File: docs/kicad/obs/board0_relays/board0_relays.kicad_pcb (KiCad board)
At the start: 2 copper layers, 100.3 x 91.4 mm, 45 parts, among them J1 INST_POWER, J10 12V_TEST, J11 5V_TEST, J12 SN65HVD230, J13 CAN_TERMINATOR, J14 MAX3232, J15 GPS_IN, J2 NMEA2000, J3 NMEA2000, J4 83A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

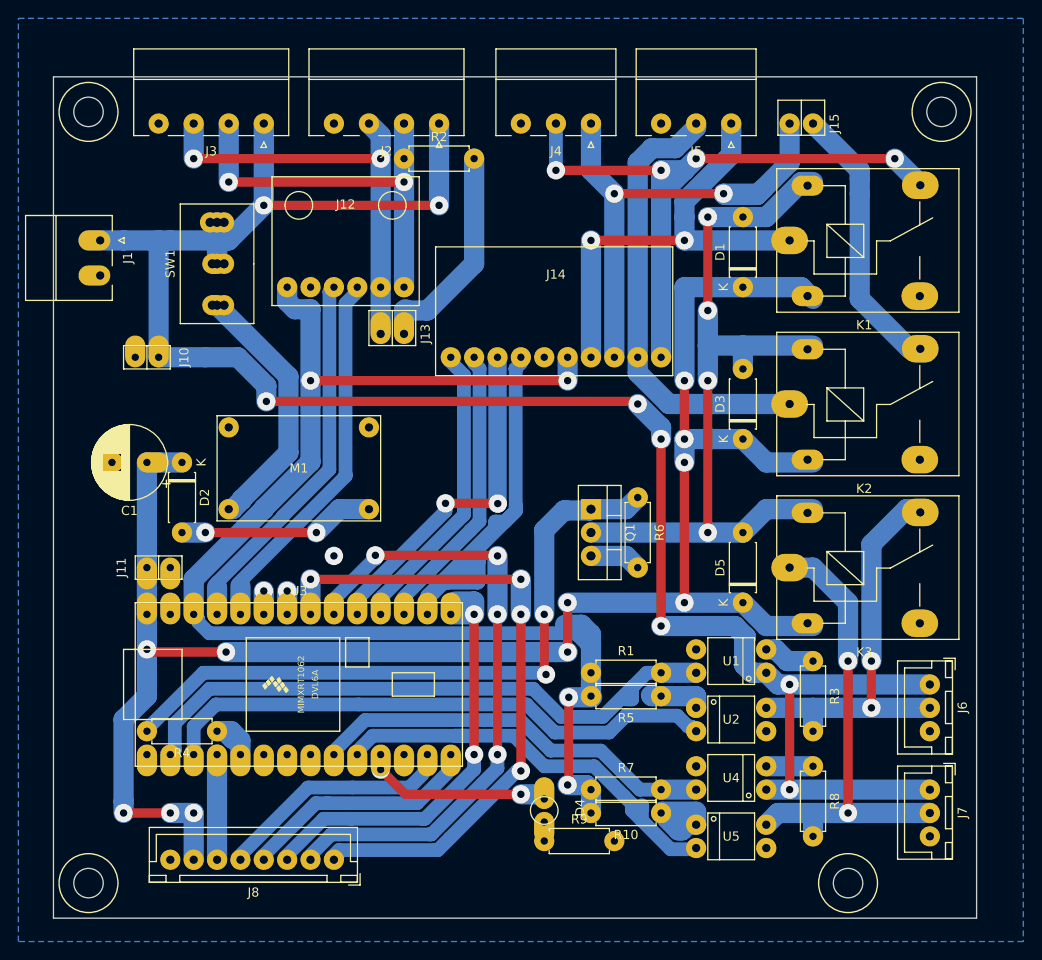
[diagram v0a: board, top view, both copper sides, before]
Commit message: create actual boat teensyBoat pcb board1;  move other kicad stuff to _obs; add/fix kicad footprints
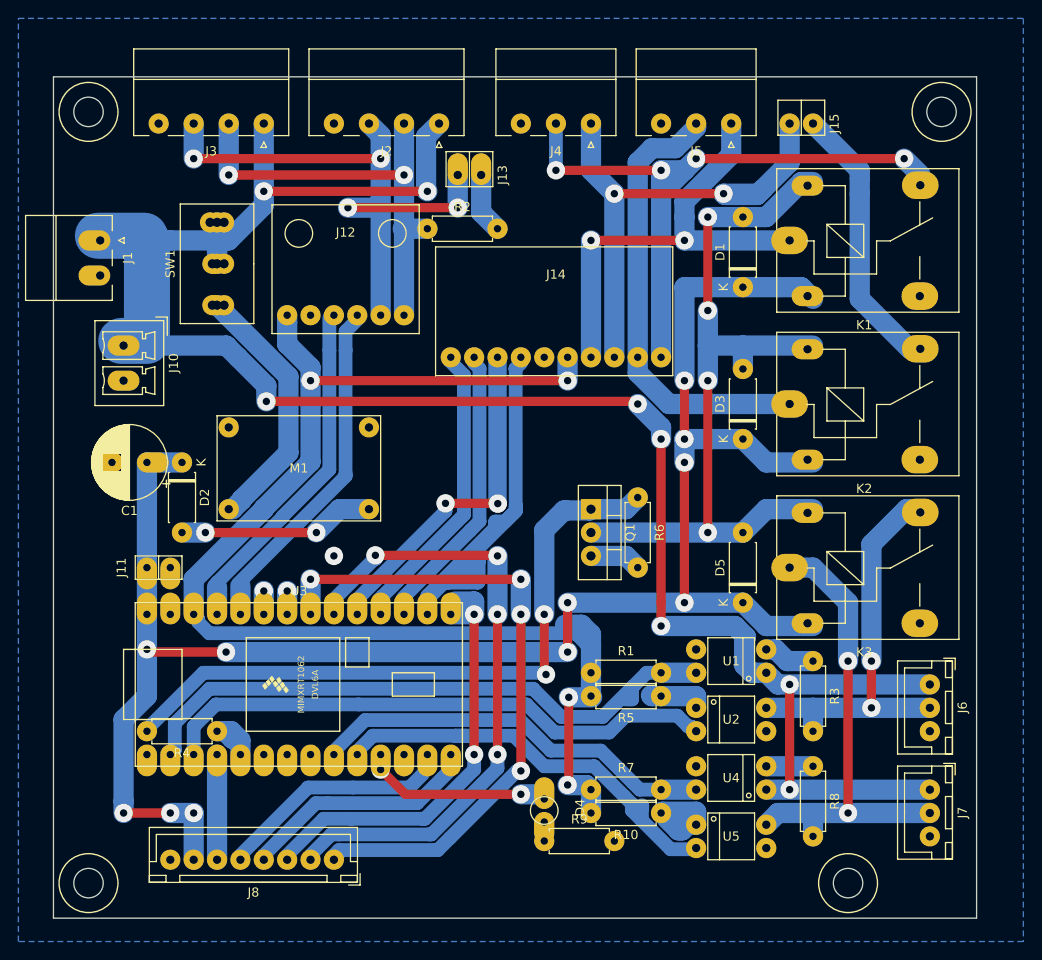
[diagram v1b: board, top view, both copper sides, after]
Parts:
- J1: value INST_POWER -> ST_PWR
- J10: value 12V_TEST -> ST_12V; footprint 0_my_footprints2:pinSocket1x2 -> 0_my_footprints:myPhoenix2x3.81_vertical
- moved J13 19.2 mm to (27.4, 42.4)
- moved R2 8.03 mm to (21.6, 48.3)
- moved J10 4.02 mm to (-11.4, 61.0)
- moved J12 3.05 mm to (12.7, 57.7)
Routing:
- net CANH: track 47.5 -> 64.7 mm, vias 2 -> 4
- net Net-(J13-Pad1): track 23.0 -> 6.58 mm
- net CANL: track 43.2 -> 48.1 mm
- net +3V3: track 148.5 -> 144.5 mm
- net CRX: track 40.3 -> 36.8 mm
- net CTX: track 43.8 -> 40.3 mm
- net 83A_IN: track 69.3 -> 68.7 mm
